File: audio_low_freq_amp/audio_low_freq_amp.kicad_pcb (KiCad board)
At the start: 2 copper layers, 40 x 40 mm, 57 parts, among them J1 Conn_01x01_Pin, J2 Conn_01x01_Pin, J3 Conn_01x01_Pin, J4 Conn_01x01_Pin, J5 Conn_01x01_Pin, Q1 PNP, Q10 NPN, Q11 PNP, Q12 NPN, Q13 PNP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

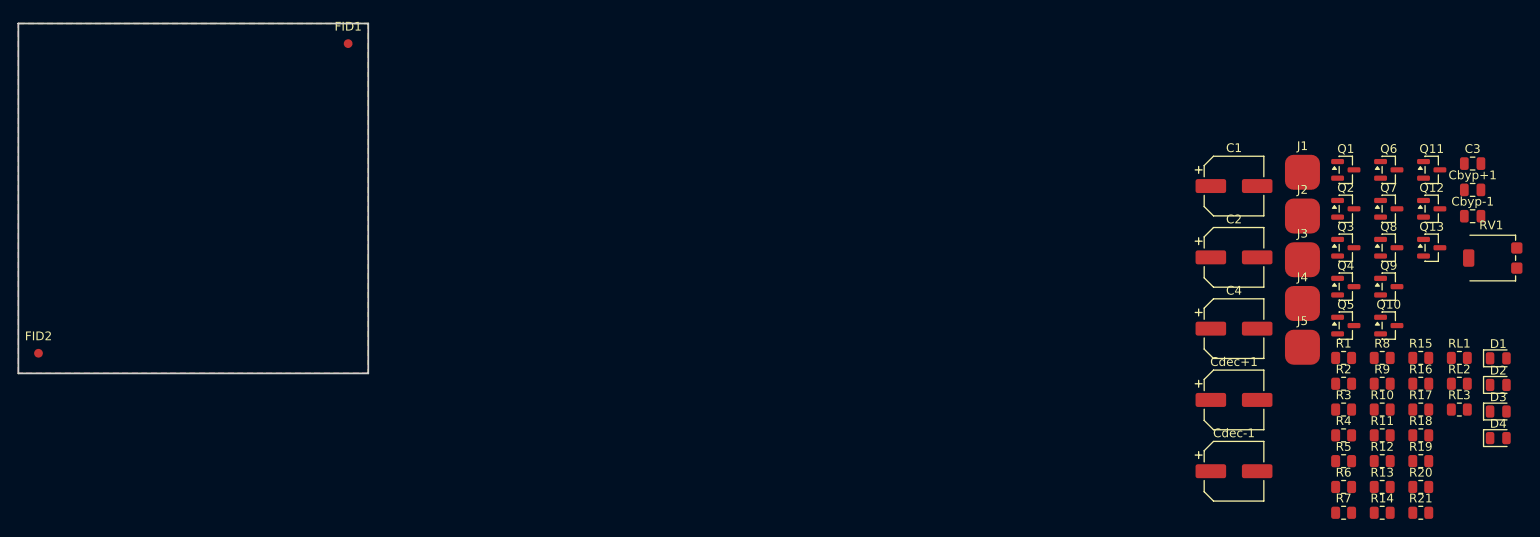
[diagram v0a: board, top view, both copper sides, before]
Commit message: layed out the parts on pcb, next is routing
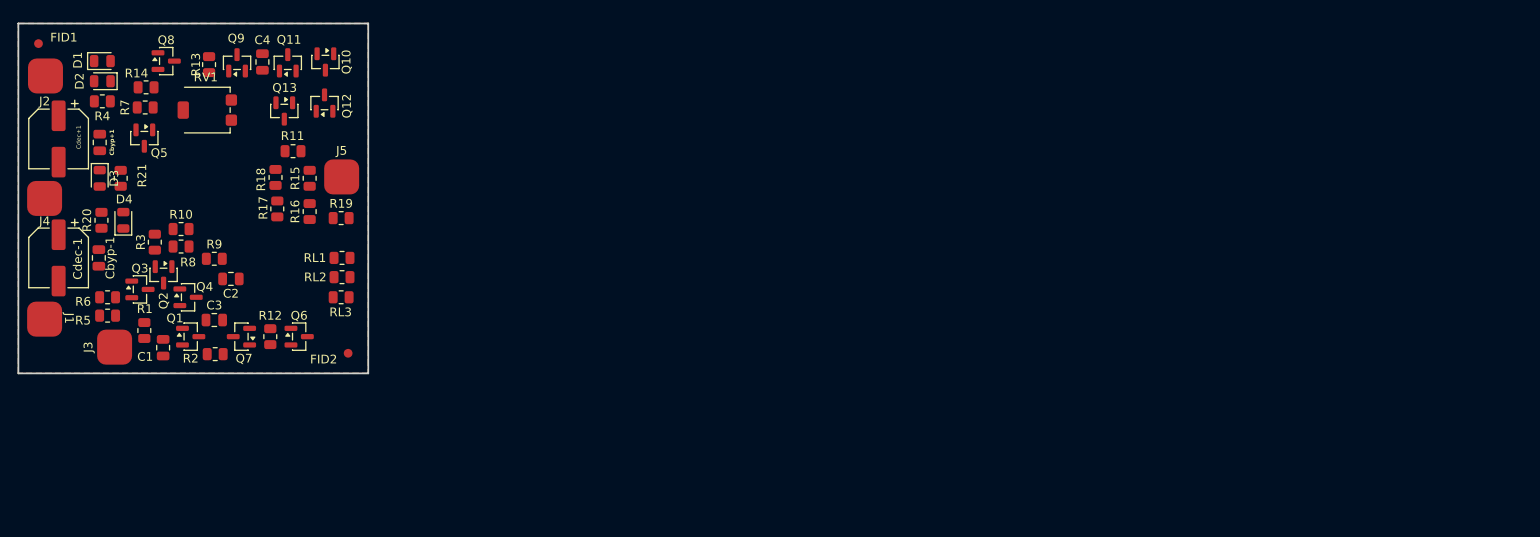
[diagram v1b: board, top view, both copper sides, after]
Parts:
- C1, C2, C4: value 10u -> 4.7u; footprint my_lib_Radu:10uF_smd_6.3x5.4_Radu -> Capacitor_SMD:C_0805_2012Metric
- moved D2 163.3 mm to (89.6, 86.6), turned to 180 degrees
- moved D1 163.2 mm to (89.6, 84.3)
- moved D3 162.1 mm to (89.3, 97.7), turned to -90 degrees
- moved D4 159.1 mm to (92.0, 102.5), turned to 90 degrees
- moved Cbyp-1 157.1 mm to (89.2, 106.8), turned to 90 degrees
- moved Cbyp+1 157.0 mm to (89.3, 93.6), turned to -90 degrees
- moved R20 153.9 mm to (89.5, 102.5), turned to 90 degrees
- moved R21 153.5 mm to (91.7, 97.7), turned to -90 degrees
- moved R14 149.4 mm to (94.6, 87.3)
- moved RV1 147.9 mm to (101.6, 89.9)
- moved R4 147.0 mm to (89.6, 88.9)
- moved C3 145.0 mm to (102.4, 113.9)
- moved J1 144.8 mm to (83.0, 113.8), turned to -90 degrees
- moved R7 144.6 mm to (94.5, 89.6), turned to 180 degrees
- moved J2 144.6 mm to (83.1, 86.0)
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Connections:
- Cdec-1 pad 1: -20V -> GND
- Cdec-1 pad 2: GND -> -20V
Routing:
- net /VIN: track 0.00 -> 1.70 mm

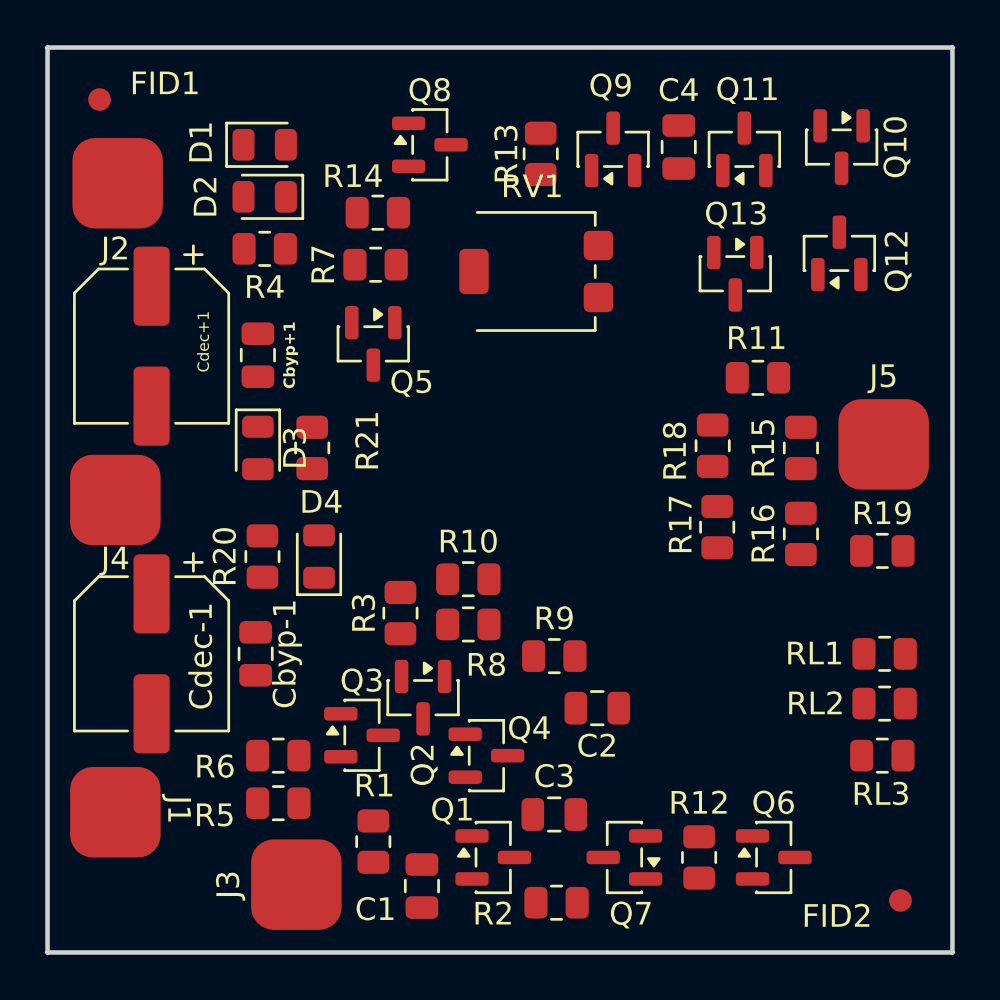
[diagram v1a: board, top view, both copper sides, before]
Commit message: made some placing adjustments. should be ready for first routing stage
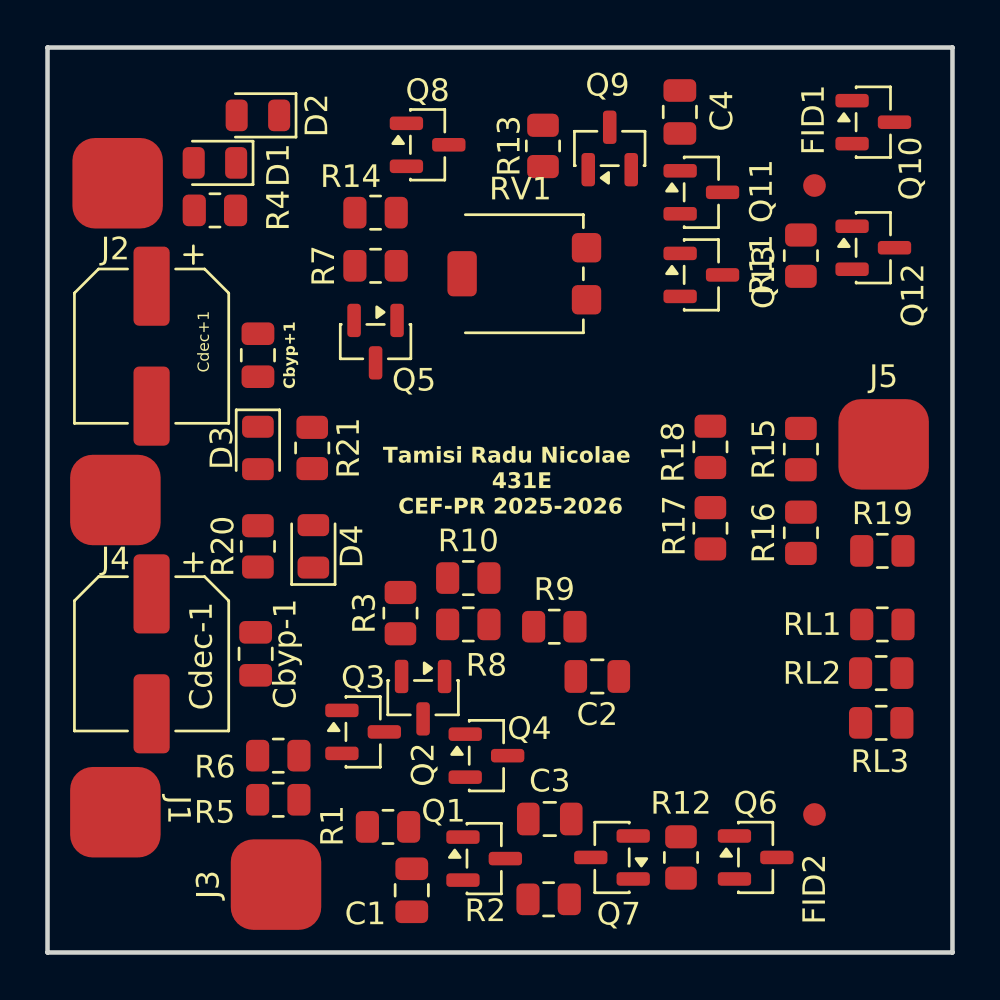
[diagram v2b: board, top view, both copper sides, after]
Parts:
- moved FID1 31.8 mm to (113.9, 86.1)
- moved R11 5.72 mm to (113.3, 89.2), turned to 90 degrees
- moved FID2 5.37 mm to (113.9, 113.9)
- moved D2 3.61 mm to (89.3, 83.0)
- moved R4 2.78 mm to (87.4, 87.2)
- moved Q11 2.69 mm to (108.9, 86.4), turned to 0 degrees
- moved D1 2.34 mm to (87.4, 85.1), turned to 180 degrees
- moved Q10 1.78 mm to (116.5, 83.3), turned to 0 degrees
- moved C4 1.55 mm to (108.0, 82.8)
- moved Q12 1.52 mm to (116.5, 88.8), turned to 0 degrees
- moved Q13 1.50 mm to (108.9, 90.0), turned to 0 degrees
- moved RL3 1.45 mm to (116.8, 109.8)
- moved C2 1.40 mm to (104.3, 107.8)
- moved RL2 1.36 mm to (116.8, 107.7)
- moved RL1 1.30 mm to (116.9, 105.5)
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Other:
- board text added: "Tamisi Radu Nicolae 431E CEF-PR 2025-2026"

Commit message: finished first iteration of routing
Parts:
- moved RL1 1.14 mm to (115.9, 104.9), turned to 90 degrees
- renumbered J2 to +20V, J1 to -20V, J4 to GND, J3 to VIN, J5 to VOUT
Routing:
- net -20V: track 0.00 -> 66.0 mm, vias 0 -> 5
- net +20V: track 0.14 -> 49.9 mm, vias 0 -> 7
- net Net-(Q11-B): track 0.00 -> 45.6 mm, vias 0 -> 2
- net Net-(Q5-C): track 0.00 -> 29.6 mm, vias 0 -> 2
- net /Vout: track 0.00 -> 24.6 mm
- net Net-(Q10-B): track 0.00 -> 19.1 mm
- net Net-(Q1-C): track 0.00 -> 17.2 mm
- net Net-(Q11-E): track 0.00 -> 12.0 mm, vias 0 -> 2
- net Net-(Q13-E): track 0.00 -> 8.56 mm
- net Net-(D2-K): track 0.00 -> 8.20 mm
- net Net-(Q5-E): track 0.00 -> 8.20 mm
- net Net-(Q12-E): track 0.00 -> 7.97 mm
- net Net-(Q4-E): track 0.00 -> 7.76 mm
- net Net-(R16-Pad1): track 0.00 -> 6.82 mm
- net Net-(Q2-C): track 0.00 -> 6.36 mm
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- added copper zone on F.Cu, net +20V
- added copper zone on F.Cu, net -20V
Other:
- board text added: "Tamisi Radu Nicolae 431E CEF-AAF 2025-2026"
- board text removed: "Tamisi Radu Nicolae 431E CEF-PR 2025-2026"

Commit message: moved fiducial fid2 to be diagonally oposed with the first and made adjustments to traces and pours
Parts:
- moved FID1 28.8 mm to (85.1, 85.1)
- moved Q10 5.61 mm to (110.9, 82.8)
- moved Q12 4.84 mm to (114.5, 84.4), turned to 90 degrees
- moved R11 3.26 mm to (111.8, 86.3)
- moved -20V 3.20 mm to (83.0, 117.0)
- moved Cdec-1 3.10 mm to (84.5, 109.9)
- moved +20V 2.95 mm to (83.0, 89.0)
- moved GND 2.90 mm to (83.0, 102.9)
- moved Cdec+1 2.65 mm to (84.6, 95.8)
- moved D1 1.92 mm to (89.3, 85.2), turned to 0 degrees
- moved R4 1.89 mm to (89.3, 87.2), turned to 180 degrees
- moved R20 1.82 mm to (89.4, 103.9)
- moved Cbyp-1 1.82 mm to (89.3, 108.6)
- moved D4 1.82 mm to (91.8, 103.9)
- moved FID2 1.44 mm to (114.9, 114.9)
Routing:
- net Net-(Q10-B): track 19.1 -> 11.3 mm
- net -20V: track 66.0 -> 60.0 mm, vias 5 -> 9
- net Net-(Q12-E): track 7.97 -> 12.4 mm
- net Net-(Q10-E): track 6.07 -> 1.76 mm
- net +20V: track 49.9 -> 46.9 mm, vias 7 -> 9
- net Net-(Q11-E): track 12.0 -> 12.6 mm
- net GND: vias 48 -> 31
- added copper zone on B.Cu, net +20V
- added copper zone on B.Cu, net -20V

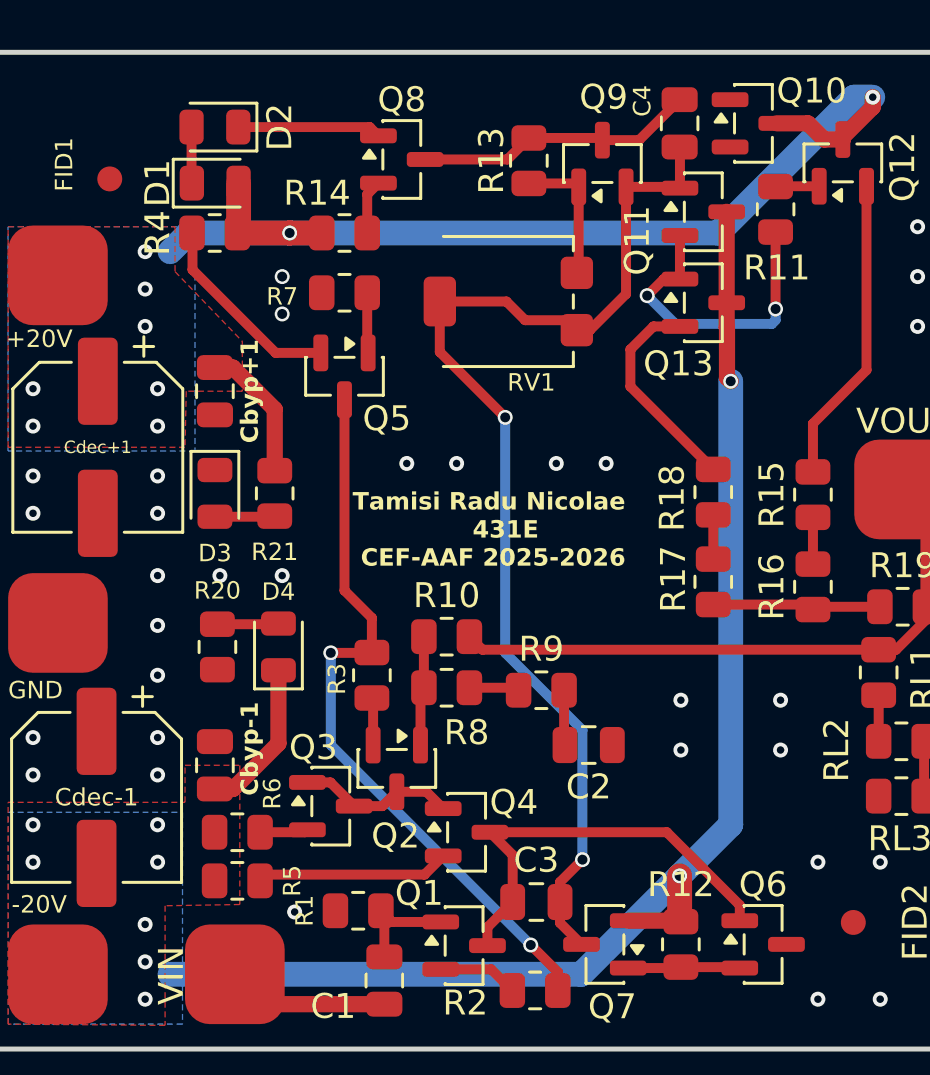
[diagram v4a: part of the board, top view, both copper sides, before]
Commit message: found some unconnected traces and resolved; still have some insignificant errors (2) about not having minimum 2 spokes for thermal relief
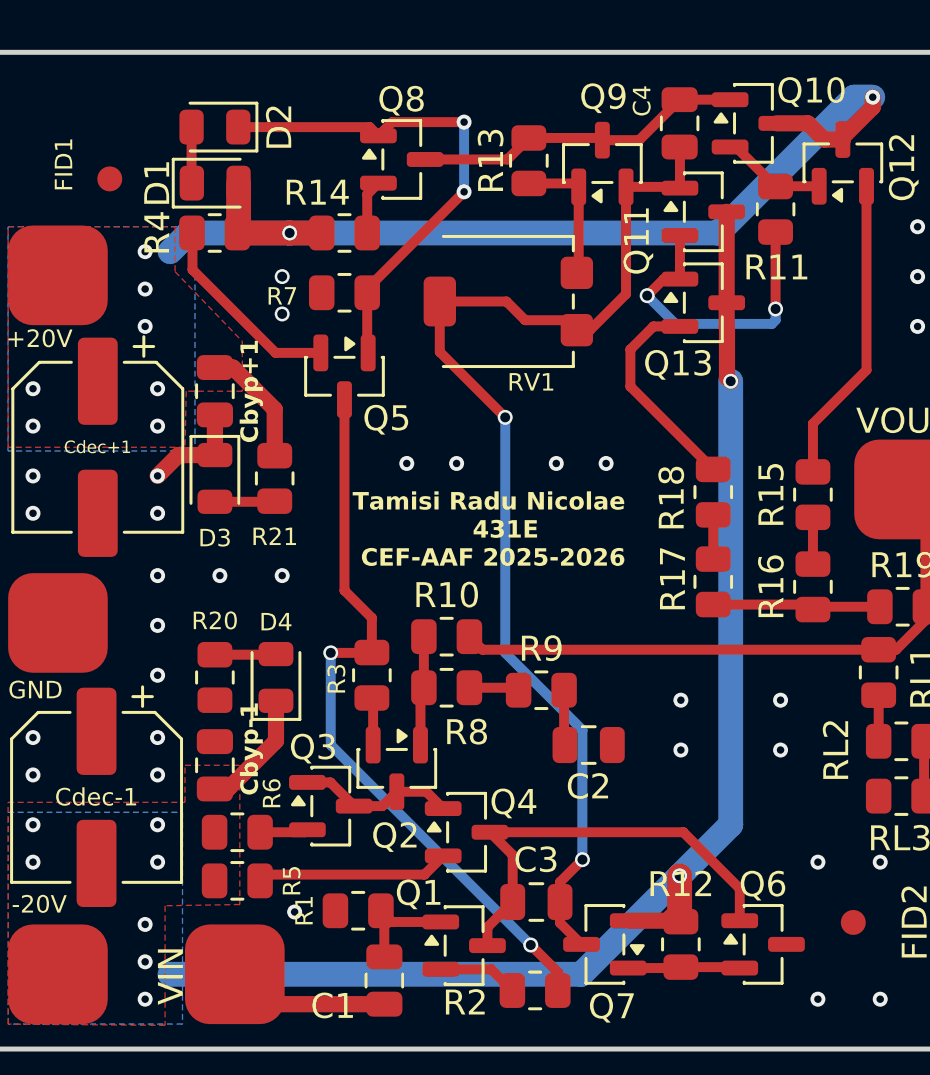
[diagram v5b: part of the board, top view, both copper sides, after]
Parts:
- moved R20 1.23 mm to (89.3, 105.1)
- moved D4 1.23 mm to (91.8, 105.1)
- moved D3 0.60 mm to (89.3, 97.1)
- moved R21 0.60 mm to (91.7, 97.1)
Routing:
- net Net-(D2-K): track 8.20 -> 20.3 mm, vias 0 -> 2
- net GND: track 0.13 -> 4.39 mm
- net Net-(Q10-E): track 1.76 -> 4.24 mm
- net Net-(Q10-B): track 11.3 -> 13.3 mm
- net -20V: track 60.0 -> 58.6 mm
- net +20V: track 46.9 -> 46.3 mm
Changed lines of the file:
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@@
 	(footprint "Resistor_SMD:R_0805_2012Metric"
 		(layer "F.Cu")
-		(at 89.4 103.8625 90)
+		(at 89.3 105.0875 90)
 		(descr "Resistor SMD 0805 (2012 Metric), square (rectangular) end terminal, IPC-7351 nominal, (Body size source: IPC-SM-782 page 72, https://www.pcb-3d.com/wordpress/wp-content/uploads/ipc-sm-782a_amendment_1_and_2.pdf), generated with kicad-footprint-generator")
 		(tags "resistor")
@@
 	(footprint "Resistor_SMD:R_0805_2012Metric"
 		(layer "F.Cu")
-		(at 91.7 97.7 -90)
+		(at 91.7 97.1 -90)
 		(descr "Resistor SMD 0805 (2012 Metric), square (rectangular) end terminal, IPC-7351 nominal, (Body size source: IPC-SM-782 page 72, https://www.pcb-3d.com/wordpress/wp-content/uploads/ipc-sm-782a_amendment_1_and_2.pdf), generated with kicad-footprint-generator")
 		(tags "resistor")
@@
 	(footprint "LED_SMD:LED_0805_2012Metric"
 		(layer "F.Cu")
-		(at 89.3 97.7 -90)
+		(at 89.3 97.1 -90)
 		(descr "LED SMD 0805 (2012 Metric), square (rectangular) end terminal, IPC-7351 nominal, (Body size source: https://docs.google.com/spreadsheets/d/1BsfQQcO9C6DZCsRaXUlFlo91Tg2WpOkGARC1WS5S8t0/edit?usp=sharing), generated with kicad-footprint-generator")
 		(tags "LED")
@@
 	(footprint "LED_SMD:LED_0805_2012Metric"
 		(layer "F.Cu")
-		(at 91.85 103.8625 90)
+		(at 91.75 105.0875 90)
 		(descr "LED SMD 0805 (2012 Metric), square (rectangular) end terminal, IPC-7351 nominal, (Body size source: https://docs.google.com/spreadsheets/d/1BsfQQcO9C6DZCsRaXUlFlo91Tg2WpOkGARC1WS5S8t0/edit?usp=sharing), generated with kicad-footprint-generator")
 		(tags "LED")
@@
 	)
 	(segment
+		(start 87.8375 96.1625)
+		(end 87 97)
+		(width 0.65)
+		(layer "F.Cu")
+		(net 4)
+	)
+	(segment
+		(start 89.3 96.1625)
+		(end 89.3 94.55)
+		(width 0.65)
+		(layer "F.Cu")
+		(net 4)
+	)
+	(segment
+		(start 89.3 96.1625)
+		(end 87.8375 96.1625)
+		(width 0.65)
+		(layer "F.Cu")
+		(net 4)
+	)
+	(segment
 		(start 116 109.85)
 		(end 116.05 109.8)
@@
 	)
 	(segment
-		(start 110.3625 114.223649)
-		(end 107.438851 111.3)
+		(start 100.2375 115.85)
+		(end 100.2375 115.1125)
 		(width 0.4)
 		(layer "F.Cu")
@@
 	)
 	(segment
-		(start 100.2375 115.85)
-		(end 100.2375 115.1125)
+		(start 110.3625 114.85)
+		(end 110.3625 113.5625)
 		(width 0.4)
 		(layer "F.Cu")
@@
 	)
 	(segment
-		(start 101.25 112.2125)
-		(end 100.3375 111.3)
+		(start 110.3625 113.5625)
+		(end 108.1 111.3)
 		(width 0.4)
 		(layer "F.Cu")
@@
 	)
 	(segment
-		(start 107.438851 111.3)
+		(start 101.25 112.2125)
 		(end 100.3375 111.3)
 		(width 0.4)
@@
 	)
 	(segment
-		(start 100.2375 115.1125)
-		(end 101.25 114.1)
+		(start 108.1 111.3)
+		(end 100.3375 111.3)
 		(width 0.4)
 		(layer "F.Cu")
@@
 	)
 	(segment
-		(start 110.3625 114.85)
-		(end 110.3625 114.223649)
+		(start 100.2375 115.1125)
+		(end 101.25 114.1)
 		(width 0.4)
 		(layer "F.Cu")
@@
 	)
 	(segment
+		(start 109.975 81.9)
+		(end 107.95 81.9)
+		(width 0.4)
+		(layer "F.Cu")
+		(net 7)
+	)
+	(segment
 		(start 106.325 83.525)
 		(end 107.95 81.9)
@@
 	)
 	(segment
+		(start 91.7 94.325)
+		(end 91.7 96.1875)
+		(width 0.65)
+		(layer "F.Cu")
+		(net 8)
+	)
+	(segment
 		(start 114.5 83.5)
 		(end 113.75 83.5)
@@
 	)
 	(segment
-		(start 91.7 94.325)
-		(end 91.7 96.7875)
-		(width 0.65)
-		(layer "F.Cu")
-		(net 8)
-	)
-	(segment
 		(start 115.7 81.8)
 		(end 115.7 82.2)
@@
 	)
 	(segment
-		(start 89.3 109.5625)
-		(end 90.025 109.5625)
+		(start 89.825 109.5625)
+		(end 91.75 107.6375)
 		(width 0.65)
 		(layer "F.Cu")
@@
 	)
 	(segment
-		(start 90.025 109.5625)
-		(end 91.85 107.7375)
-		(width 0.65)
-		(layer "F.Cu")
-		(net 9)
-	)
-	(segment
 		(start 107.95 113.05)
 		(end 107.95 114.8375)
@@
 	)
 	(segment
-		(start 91.85 107.7375)
-		(end 91.85 104.8)
+		(start 91.75 107.6375)
+		(end 91.75 106.025)
 		(width 0.65)
 		(layer "F.Cu")
@@
 	)
 	(segment
+		(start 89.3 109.5625)
+		(end 89.825 109.5625)
+		(width 0.65)
+		(layer "F.Cu")
+		(net 9)
+	)
+	(segment
 		(start 110 93.2)
 		(end 109.85 93.05)
@@
 	)
 	(segment
+		(start 96.4125 82.8)
+		(end 95.8625 83.35)
+		(width 0.4)
+		(layer "F.Cu")
+		(net 11)
+	)
+	(segment
 		(start 95.4125 89.65)
 		(end 95.4125 92.025)
@@
 	)
 	(segment
+		(start 95.4125 89.65)
+		(end 95.4125 89.4875)
+		(width 0.4)
+		(layer "F.Cu")
+		(net 11)
+	)
+	(segment
 		(start 95.5125 83)
 		(end 95.8625 83.35)
@@
 	)
 	(segment
+		(start 99.3 82.8)
+		(end 96.4125 82.8)
+		(width 0.4)
+		(layer "F.Cu")
+		(net 11)
+	)
+	(segment
 		(start 90.2375 83)
 		(end 95.5125 83)
@@
 	)
 	(segment
-		(start 89.3 98.6375)
-		(end 91.675 98.6375)
+		(start 95.4125 89.4875)
+		(end 99.3 85.6)
+		(width 0.4)
+		(layer "F.Cu")
+		(net 11)
+	)
+	(via
+		(at 99.3 82.8)
+		(size 0.6)
+		(drill 0.3)
+		(layers "F.Cu" "B.Cu")
+		(net 11)
+	)
+	(via
+		(at 99.3 85.6)
+		(size 0.6)
+		(drill 0.3)
+		(layers "F.Cu" "B.Cu")
+		(net 11)
+	)
+	(segment
+		(start 99.3 85.6)
+		(end 99.3 82.8)
+		(width 0.4)
+		(layer "B.Cu")
+		(net 11)
+	)
+	(segment
+		(start 89.3 98.0375)
+		(end 91.675 98.0375)
 		(width 0.4)
 		(layer "F.Cu")
@@
 	)
 	(segment
-		(start 91.675 98.6375)
-		(end 91.7 98.6125)
+		(start 91.675 98.0375)
+		(end 91.7 98.0125)
 		(width 0.4)
 		(layer "F.Cu")
@@
 	)
 	(segment
-		(start 89.4 102.95)
-		(end 91.825 102.95)
+		(start 91.725 104.175)
+		(end 91.75 104.15)
 		(width 0.4)
 		(layer "F.Cu")
@@
 	)
 	(segment
-		(start 91.825 102.95)
-		(end 91.85 102.925)
+		(start 89.3 104.175)
+		(end 91.725 104.175)
 		(width 0.4)
 		(layer "F.Cu")
@@
 	)
 	(segment
+		(start 109.975 83.8)
+		(end 110.2125 83.8)
+		(width 0.4)
+		(layer "F.Cu")
+		(net 26)
+	)
+	(segment
 		(start 113.55 85.375)
 		(end 111.8125 85.375)
@@
 	)
 	(segment
+		(start 110.2125 83.8)
+		(end 111.8 85.3875)
+		(width 0.4)
+		(layer "F.Cu")
+		(net 26)
+	)
+	(segment
 		(start 111.8125 85.375)
 		(end 111.8 85.3875)
@@
 		(fill yes
 			(thermal_gap 0.5)
-			(thermal_bridge_width 1)
+			(thermal_bridge_width 0.7)
+			(smoothing fillet)
 		)
 		(polygon
@@
 			(thermal_gap 0.5)
 			(thermal_bridge_width 1)
+			(smoothing fillet)
 		)
 		(polygon
@@
 			(thermal_gap 0.5)
 			(thermal_bridge_width 1)
+			(smoothing fillet)
 		)
 		(polygon
